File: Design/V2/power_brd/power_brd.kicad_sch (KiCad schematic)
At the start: 41 parts, among them J1 XT60PW-M, U1 TPS5430DDAR, U2 TPS5430DDAR, U3 TPS5430DDAR, U4 TPS5430DDAR, U5 TPS5430DDAR

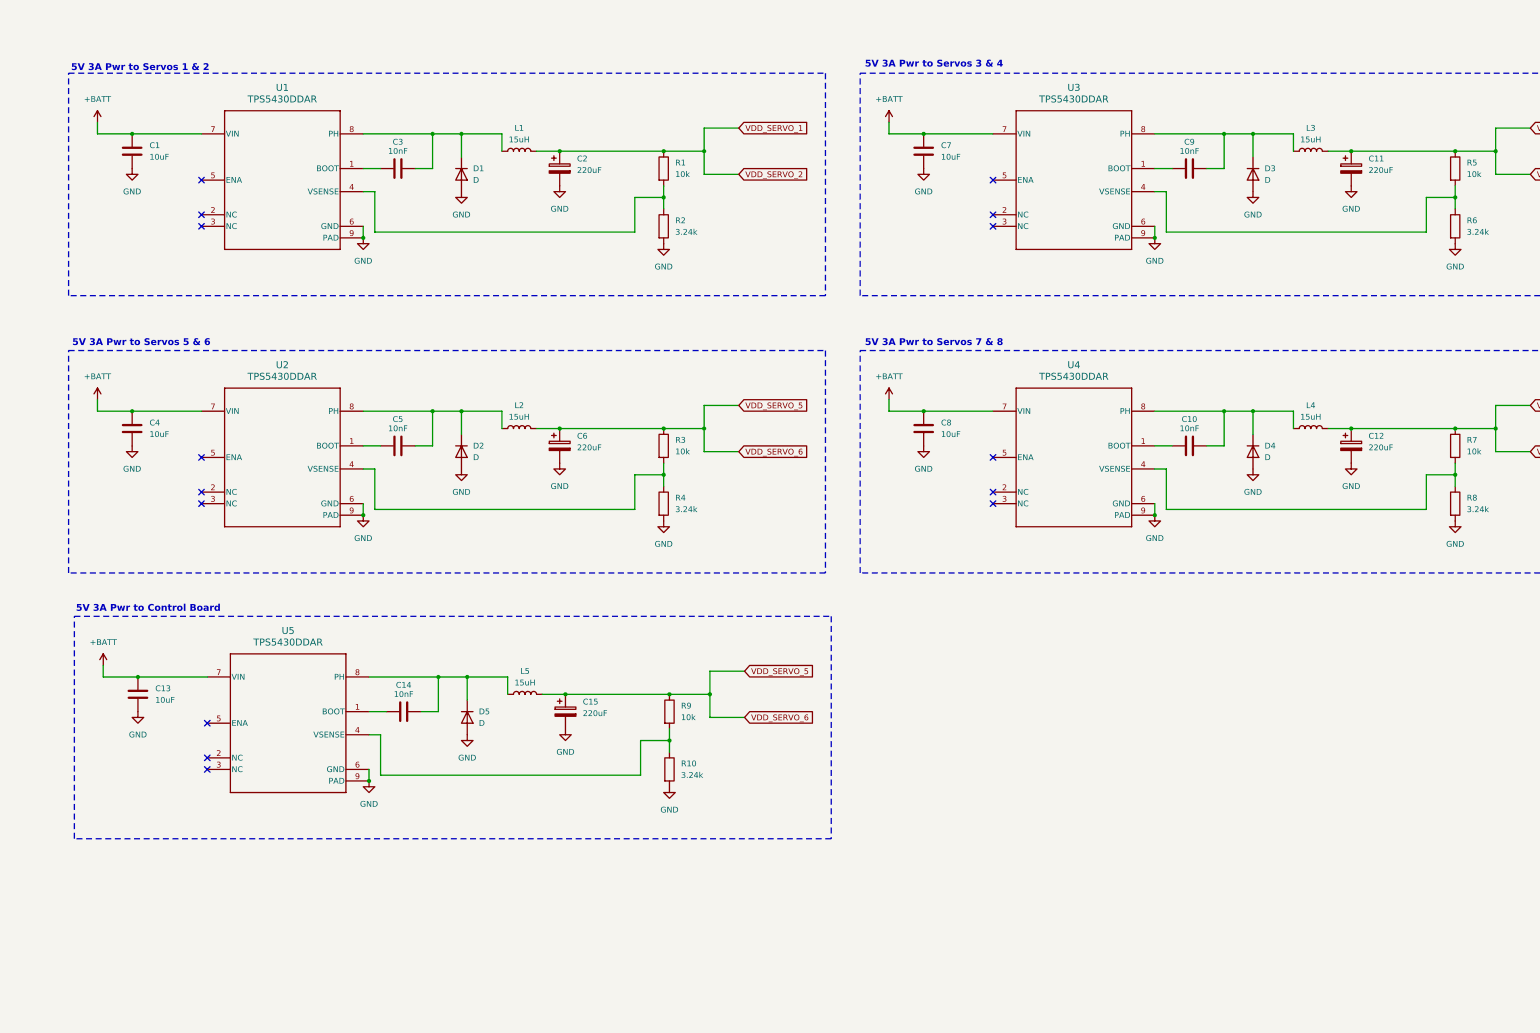
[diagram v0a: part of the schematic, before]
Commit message: started on power pcb
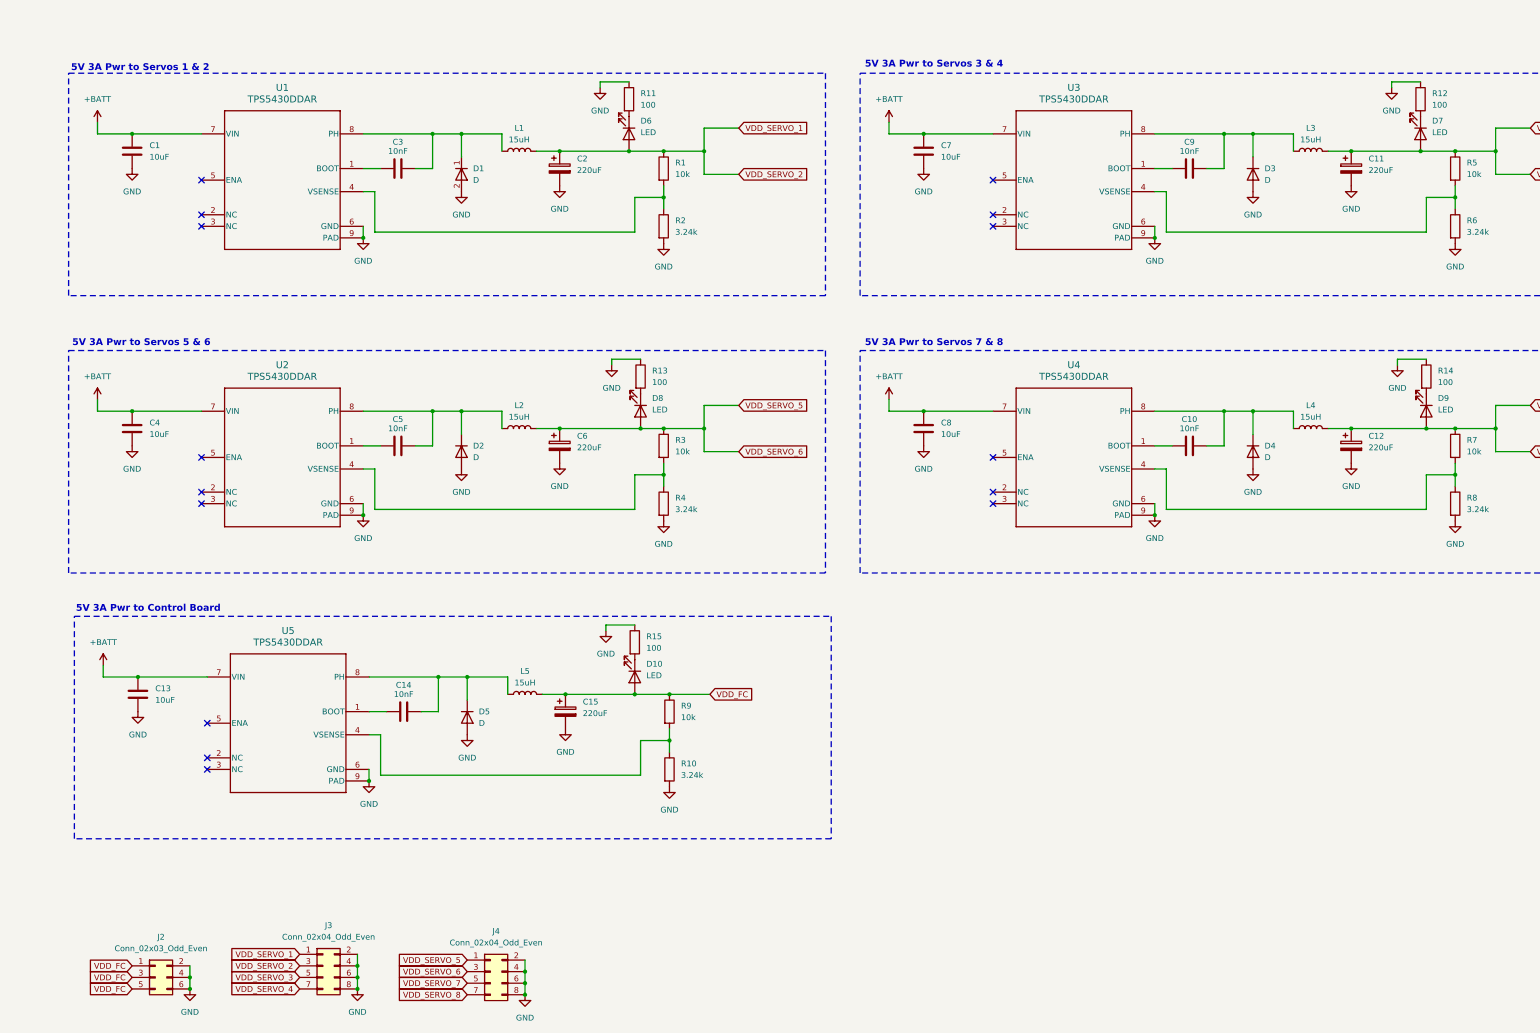
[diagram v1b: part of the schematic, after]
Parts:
- added D10, D6, D7, D8, D9: LED, LED_SMD:LED_0805_2012Metric_Pad1.15x1.40mm_HandSolder, symbol Device:LED
- added J2: Conn_02x03_Odd_Even, Connector_PinHeader_2.54mm:PinHeader_2x03_P2.54mm_Vertical, symbol Connector_Generic:Conn_02x03_Odd_Even
- added J3, J4: Conn_02x04_Odd_Even, Connector_PinHeader_2.54mm:PinHeader_2x04_P2.54mm_Vertical, symbol Connector_Generic:Conn_02x04_Odd_Even
- added R11, R12, R13, R14, R15: 100, Resistor_SMD:R_0805_2012Metric_Pad1.20x1.40mm_HandSolder, symbol Device:R
- U1, U2, U3, U4, U5: footprint DDA0008J -> Regulators:TPS5430DDAR
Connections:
- net GND: now also J2.2 (Pin_2), J2.4 (Pin_4), J2.6 (Pin_6), J3.2 (Pin_2), J3.4 (Pin_4), J3.6 (Pin_6), J3.8 (Pin_8), J4.2 (Pin_2), J4.4 (Pin_4), J4.6 (Pin_6), J4.8 (Pin_8), R11.1, R12.1, R13.1, R14.1, R15.1
- net VDD_SERVO_1: now also D6.2 (A), J3.1 (Pin_1), J3.3 (Pin_3)
- net VDD_SERVO_3: now also D7.2 (A), J3.5 (Pin_5), J3.7 (Pin_7)
- net VDD_SERVO_5: now also D8.2 (A), J4.1 (Pin_1), J4.3 (Pin_3); no longer C15.1, L5.2, R9.1
- net VDD_SERVO_7: now also D9.2 (A), J4.5 (Pin_5), J4.7 (Pin_7)
- new net: D9.1 (K), R14.2
- new net: D6.1 (K), R11.2
- new net: D10.1 (K), R15.2
- new net: D7.1 (K), R12.2
- new net: D8.1 (K), R13.2
- new net VDD_FC: C15.1, D10.2 (A), J2.1 (Pin_1), J2.3 (Pin_3), J2.5 (Pin_5), L5.2, R9.1

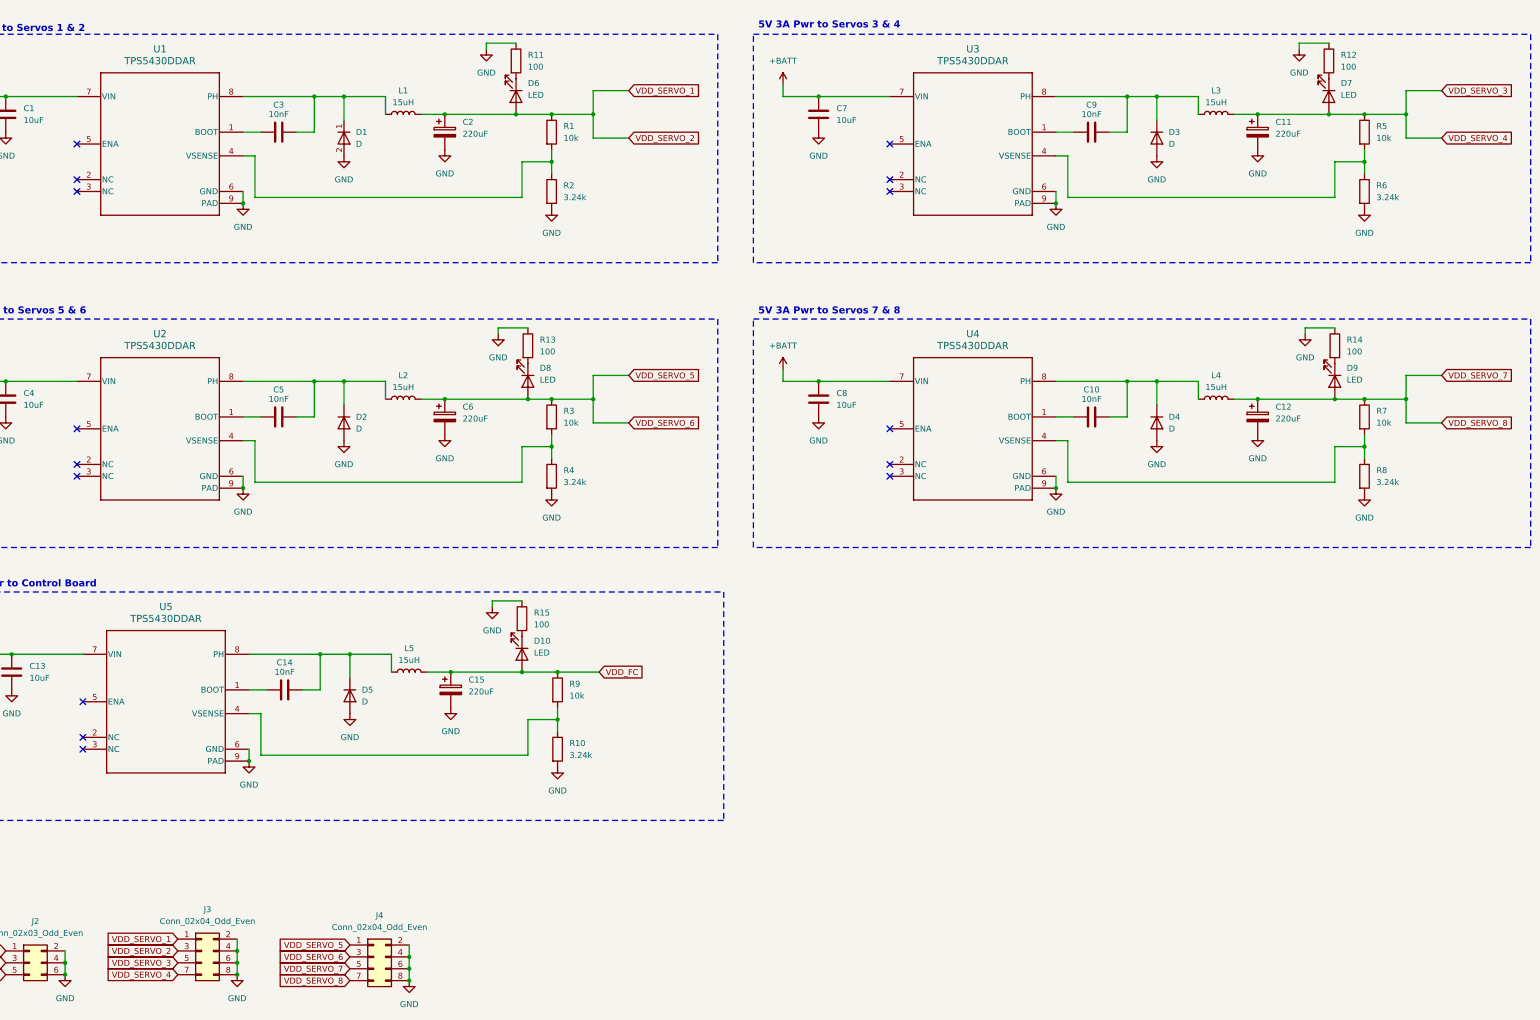
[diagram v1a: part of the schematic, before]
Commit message: laying out power board
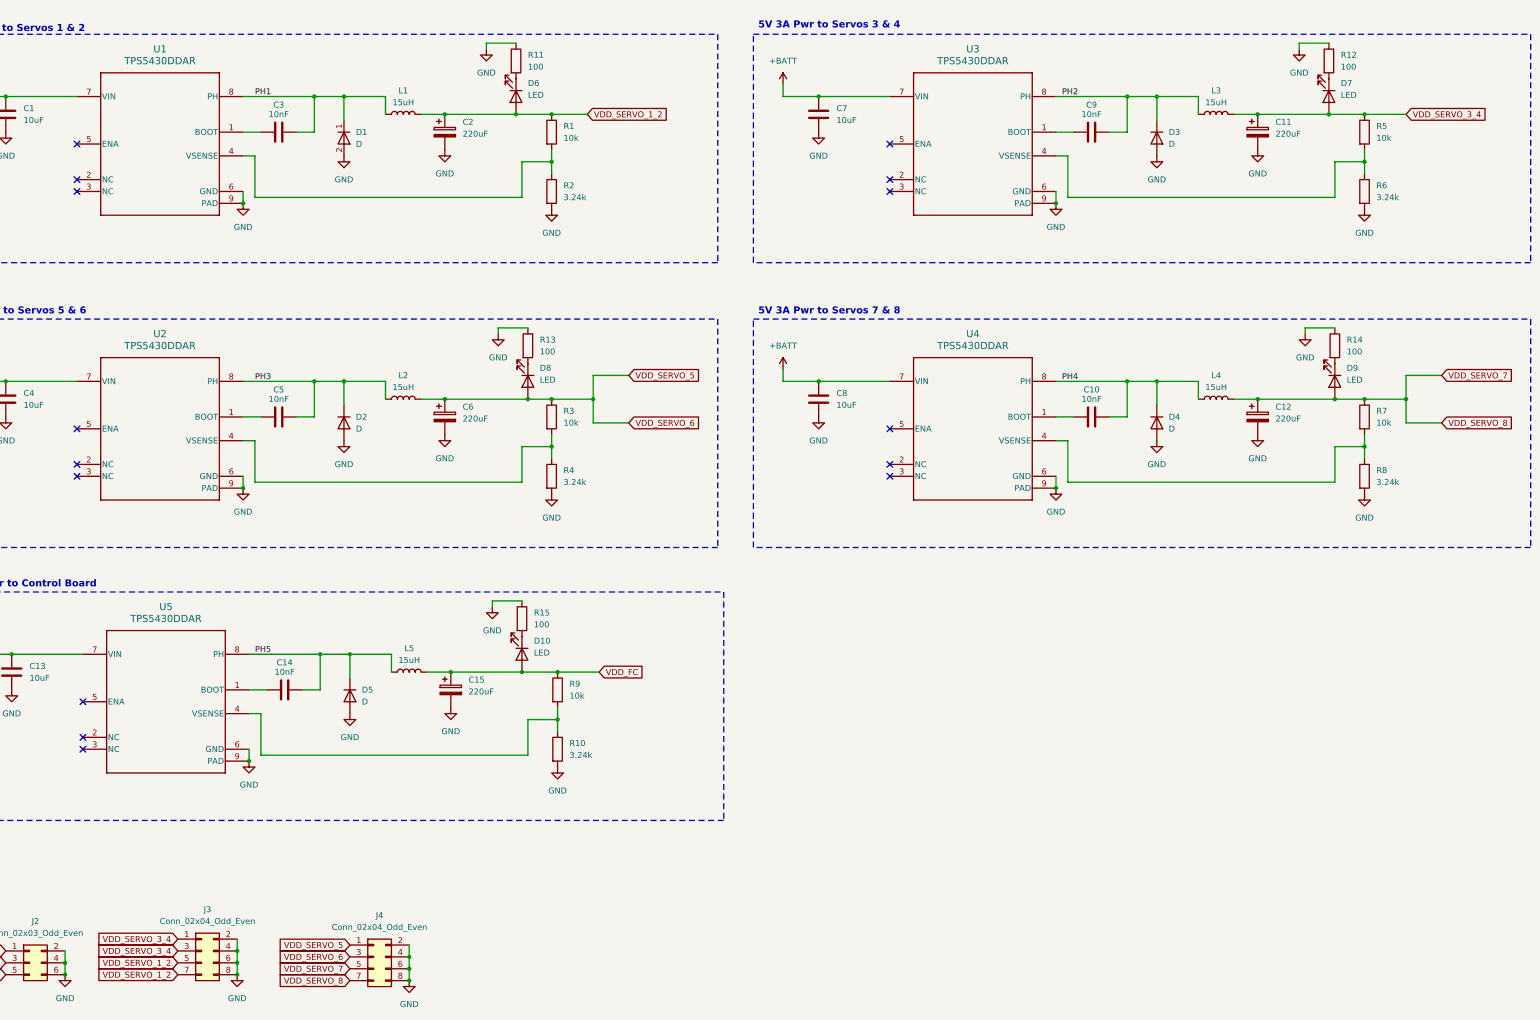
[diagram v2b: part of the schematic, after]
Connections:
- net PH3: now reaches C5.2, D2.1 (K), L2.1, U2.8 (PH)
- net PH2: now reaches C9.2, D3.1 (K), L3.1, U3.8 (PH)
- net PH1: now reaches C3.2, D1.1 (K), L1.1, U1.8 (PH)
- net PH4: now reaches C10.2, D4.1 (K), L4.1, U4.8 (PH)
- net PH5: now reaches C14.2, D5.1 (K), L5.1, U5.8 (PH)
- net VDD_SERVO_1 renamed VDD_SERVO_1_2
- net VDD_SERVO_1_2: now also J3.5 (Pin_5), J3.7 (Pin_7); no longer J3.1 (Pin_1), J3.3 (Pin_3)
- net VDD_SERVO_3 renamed VDD_SERVO_3_4
- net VDD_SERVO_3_4: now also J3.1 (Pin_1), J3.3 (Pin_3); no longer J3.5 (Pin_5), J3.7 (Pin_7)

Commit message: mostly finished power board layout
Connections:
- net VDD_SERVO_5 renamed VDD_SERVO_5_6
- net VDD_SERVO_7 renamed VDD_SERVO_7_8
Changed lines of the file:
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@@
-	)
-	(junction
-		(at 245.11 138.43)
-		(diameter 0)
-		(color 0 0 0 0)
 	)
 	(junction
@@
 	(junction
 		(at 132.08 259.08)
-		(diameter 0)
-		(color 0 0 0 0)
-	)
-	(junction
-		(at 419.1 138.43)
 		(diameter 0)
 		(color 0 0 0 0)
@@
 	(wire
 		(pts
-			(xy 419.1 143.51) (xy 419.1 138.43)
-		)
-		(stroke
-			(width 0)
-			(type default)
-		)
-	)
-	(wire
-		(pts
 			(xy 223.52 181.61) (xy 223.52 182.88)
 		)
@@
 	(wire
 		(pts
-			(xy 419.1 138.43) (xy 410.21 138.43)
+			(xy 410.21 138.43) (xy 420.37 138.43)
 		)
 		(stroke
@@
 	(wire
 		(pts
-			(xy 245.11 138.43) (xy 245.11 133.35)
-		)
-		(stroke
-			(width 0)
-			(type default)
-		)
-	)
-	(wire
-		(pts
 			(xy 182.88 200.66) (xy 186.69 200.66)
 		)
@@
 	(wire
 		(pts
-			(xy 245.11 143.51) (xy 252.73 143.51)
-		)
-		(stroke
-			(width 0)
-			(type default)
-		)
-	)
-	(wire
-		(pts
 			(xy 213.36 77.47) (xy 228.6 77.47)
 		)
@@
 	(wire
 		(pts
-			(xy 245.11 133.35) (xy 252.73 133.35)
-		)
-		(stroke
-			(width 0)
-			(type default)
-		)
-	)
-	(wire
-		(pts
 			(xy 228.6 62.23) (xy 222.25 62.23)
 		)
@@
 	(wire
 		(pts
-			(xy 419.1 143.51) (xy 426.72 143.51)
-		)
-		(stroke
-			(width 0)
-			(type default)
-		)
-	)
-	(wire
-		(pts
 			(xy 396.24 62.23) (xy 396.24 63.5)
 		)
@@
 	(wire
 		(pts
-			(xy 419.1 138.43) (xy 419.1 133.35)
-		)
-		(stroke
-			(width 0)
-			(type default)
-		)
-	)
-	(wire
-		(pts
 			(xy 236.22 148.59) (xy 229.87 148.59)
 		)
@@
 	(wire
 		(pts
-			(xy 245.11 143.51) (xy 245.11 138.43)
-		)
-		(stroke
-			(width 0)
-			(type default)
-		)
-	)
-	(wire
-		(pts
 			(xy 173.99 214.63) (xy 173.99 205.74)
 		)
@@
 		(pts
 			(xy 171.45 213.36) (xy 171.45 215.9)
-		)
-		(stroke
-			(width 0)
-			(type default)
-		)
-	)
-	(wire
-		(pts
-			(xy 419.1 133.35) (xy 426.72 133.35)
 		)
 		(stroke
@@
 			)
 			(justify left bottom)
+		)
+	)
+	(global_label "VDD_SERVO_5_6"
+		(shape input)
+		(at 193.04 257.81 180)
+		(fields_autoplaced yes)
+		(effects
+			(font
+				(size 1.27 1.27)
+			)
+			(justify right)
+		)
+		(property "Intersheetrefs" "${INTERSHEET_REFS}"
+			(at 175.0568 257.81 0)
+			(effects
+				(font
+					(size 1.27 1.27)
+				)
+				(justify right)
+				(hide yes)
+			)
 		)
 	)
@@
 		)
 	)
-	(global_label "VDD_SERVO_8"
-		(shape input)
-		(at 193.04 262.89 180)
-		(fields_autoplaced yes)
-		(effects
-			(font
-				(size 1.27 1.27)
-			)
-			(justify right)
-		)
-		(property "Intersheetrefs" "${INTERSHEET_REFS}"
-			(at 177.2339 262.89 0)
-			(effects
-				(font
-					(size 1.27 1.27)
-				)
-				(justify right)
-				(hide yes)
-			)
-		)
-	)
 	(global_label "VDD_FC"
 		(shape input)
@@
 		)
 	)
-	(global_label "VDD_SERVO_5"
+	(global_label "VDD_SERVO_5_6"
 		(shape input)
-		(at 252.73 133.35 0)
+		(at 245.11 138.43 0)
 		(fields_autoplaced yes)
 		(effects
@@
 		)
 		(property "Intersheetrefs" "${INTERSHEET_REFS}"
-			(at 268.5361 133.35 0)
+			(at 263.0932 138.43 0)
 			(effects
 				(font
@@
 				)
 				(justify left)
+				(hide yes)
+			)
+		)
+	)
+	(global_label "VDD_SERVO_7_8"
+		(shape input)
+		(at 193.04 260.35 180)
+		(fields_autoplaced yes)
+		(effects
+			(font
+				(size 1.27 1.27)
+			)
+			(justify right)
+		)
+		(property "Intersheetrefs" "${INTERSHEET_REFS}"
+			(at 175.0568 260.35 0)
+			(effects
+				(font
+					(size 1.27 1.27)
+				)
+				(justify right)
+				(hide yes)
+			)
+		)
+	)
+	(global_label "VDD_SERVO_5_6"
+		(shape input)
+		(at 193.04 255.27 180)
+		(fields_autoplaced yes)
+		(effects
+			(font
+				(size 1.27 1.27)
+			)
+			(justify right)
+		)
+		(property "Intersheetrefs" "${INTERSHEET_REFS}"
+			(at 175.0568 255.27 0)
+			(effects
+				(font
+					(size 1.27 1.27)
+				)
+				(justify right)
 				(hide yes)
 			)
@@
 		)
 	)
-	(global_label "VDD_SERVO_6"
-		(shape input)
-		(at 193.04 257.81 180)
-		(fields_autoplaced yes)
-		(effects
-			(font
-				(size 1.27 1.27)
-			)
-			(justify right)
-		)
-		(property "Intersheetrefs" "${INTERSHEET_REFS}"
-			(at 177.2339 257.81 0)
-			(effects
-				(font
-					(size 1.27 1.27)
-				)
-				(justify right)
-				(hide yes)
-			)
-		)
-	)
-	(global_label "VDD_SERVO_8"
-		(shape input)
-		(at 426.72 143.51 0)
-		(fields_autoplaced yes)
-		(effects
-			(font
-				(size 1.27 1.27)
-			)
-			(justify left)
-		)
-		(property "Intersheetrefs" "${INTERSHEET_REFS}"
-			(at 442.5261 143.51 0)
-			(effects
-				(font
-					(size 1.27 1.27)
-				)
-				(justify left)
-				(hide yes)
-			)
-		)
-	)
 	(global_label "VDD_SERVO_1_2"
 		(shape input)
@@
 		)
 	)
-	(global_label "VDD_SERVO_6"
-		(shape input)
-		(at 252.73 143.51 0)
-		(fields_autoplaced yes)
-		(effects
-			(font
-				(size 1.27 1.27)
-			)
-			(justify left)
-		)
-		(property "Intersheetrefs" "${INTERSHEET_REFS}"
-			(at 268.5361 143.51 0)
-			(effects
-				(font
-					(size 1.27 1.27)
-				)
-				(justify left)
-				(hide yes)
-			)
-		)
-	)
 	(global_label "VDD_SERVO_3_4"
 		(shape input)
@@
 		)
 	)
-	(global_label "VDD_SERVO_5"
+	(global_label "VDD_SERVO_7_8"
 		(shape input)
-		(at 193.04 255.27 180)
+		(at 420.37 138.43 0)
 		(fields_autoplaced yes)
 		(effects
@@
 				(size 1.27 1.27)
 			)
-			(justify right)
+			(justify left)
 		)
 		(property "Intersheetrefs" "${INTERSHEET_REFS}"
-			(at 177.2339 255.27 0)
-			(effects
-				(font
-					(size 1.27 1.27)
-				)
-				(justify right)
-				(hide yes)
-			)
-		)
-	)
-	(global_label "VDD_SERVO_7"
-		(shape input)
-		(at 426.72 133.35 0)
-		(fields_autoplaced yes)
-		(effects
-			(font
-				(size 1.27 1.27)
-			)
-			(justify left)
-		)
-		(property "Intersheetrefs" "${INTERSHEET_REFS}"
-			(at 442.5261 133.35 0)
+			(at 438.3532 138.43 0)
 			(effects
 				(font
@@
 		)
 	)
-	(global_label "VDD_SERVO_7"
+	(global_label "VDD_SERVO_7_8"
 		(shape input)
-		(at 193.04 260.35 180)
+		(at 193.04 262.89 180)
 		(fields_autoplaced yes)
 		(effects
@@
 		)
 		(property "Intersheetrefs" "${INTERSHEET_REFS}"
-			(at 177.2339 260.35 0)
+			(at 175.0568 262.89 0)
 			(effects
 				(font

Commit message: power board
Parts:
- added H1, H2, H3, H4: MountingHole_Pad, MountingHole:MountingHole_3.2mm_M3_Pad_Via, symbol Mechanical:MountingHole_Pad
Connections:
- net GND: now also H1.1, H2.1, H3.1, H4.1
- net VDD_SERVO_5_6: now also J4.5 (Pin_5), J4.7 (Pin_7); no longer J4.1 (Pin_1), J4.3 (Pin_3)
- net VDD_SERVO_7_8: now also J4.1 (Pin_1), J4.3 (Pin_3); no longer J4.5 (Pin_5), J4.7 (Pin_7)
